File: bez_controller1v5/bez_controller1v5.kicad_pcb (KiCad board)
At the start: 4 copper layers, 130 x 65 mm, 88 parts, among them J1 Conn_01x03_Male, J10 Conn_01x07_Socket, J11 Conn_01x03_Male, J12 Conn_01x03_Male, J13 USB_B_Mini, J14 PPTC041LGBN-RC, J15 Conn_01x03_Male, J16 MOLEX_Conn_Button, J17 MOLEX_Conn_Button, J2 Conn_01x03_Male, J3 Conn_01x03_Male, J4 Screw_Terminal_01x02, J5 Conn_01x03_Male, J6 Conn_01x03_Male, J7 Conn_01x03_Male, J8 JTAG Conn_01x06_Male, J9 Conn_01x09_Socket, U10 USBLC6-4SC6, U11 74LVC2G241, U12 74LVC2G241, U2 74LVC2G241, U3 74LVC2G241, U4 LF50ABV_TO220, U5 LD1117AS33TR_SOT223, U6 INA180A1, U7 STM32F446RETx, U8 74LVC2G241, U9 74LVC2G241, Y1 8MHz

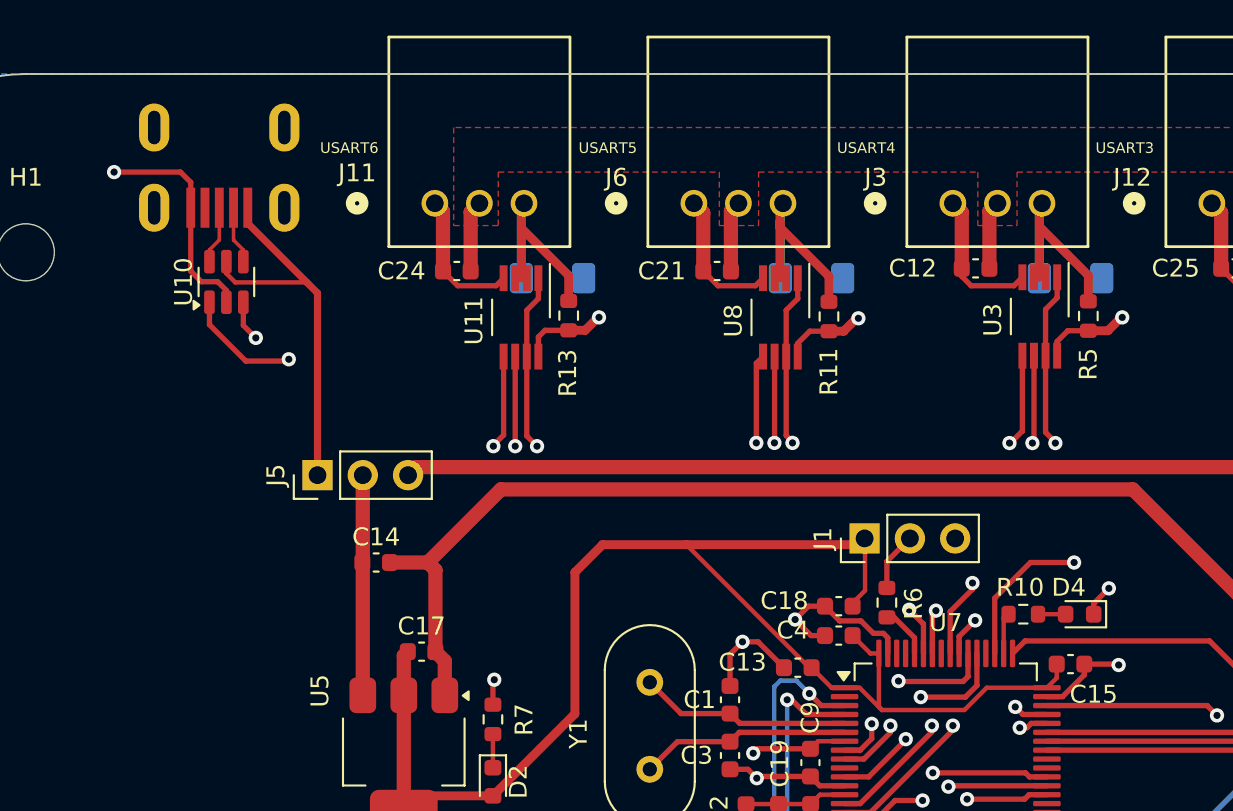
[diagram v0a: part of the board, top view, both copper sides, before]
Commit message: Verified circuit; also added button as per Nam's request
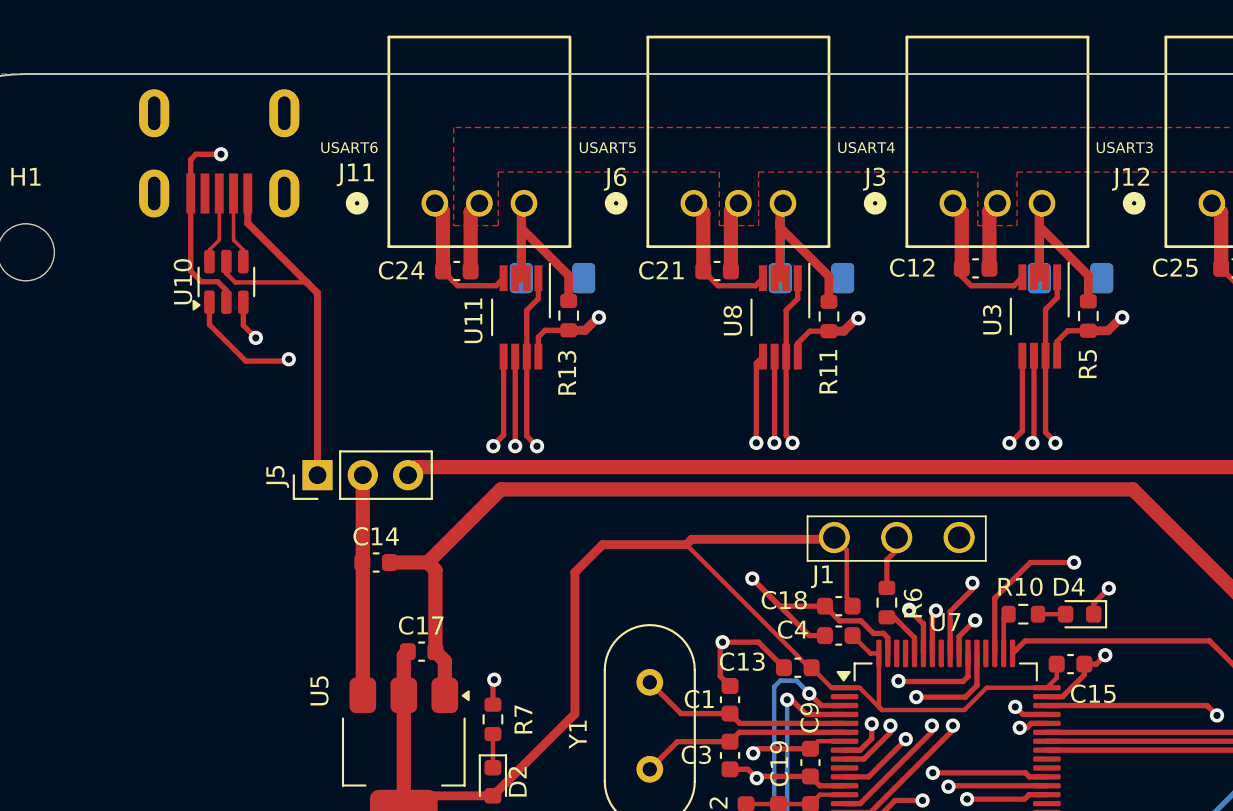
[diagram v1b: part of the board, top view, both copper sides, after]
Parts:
- J1: footprint Connector_PinHeader_2.54mm:PinHeader_1x03_P2.54mm_Vertical -> KiCad:BootloaderButton
- moved J1 3.30 mm to (142.6, 71.8), turned to 0 degrees
- moved J13 0.80 mm to (104.6, 47.1)
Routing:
- net GND: track 125.5 -> 130.7 mm
- net /USART1_DIR: track 64.7 -> 66.0 mm
- net +3.3V: track 299.7 -> 298.6 mm
- net /USART3_RX: track 37.0 -> 36.0 mm

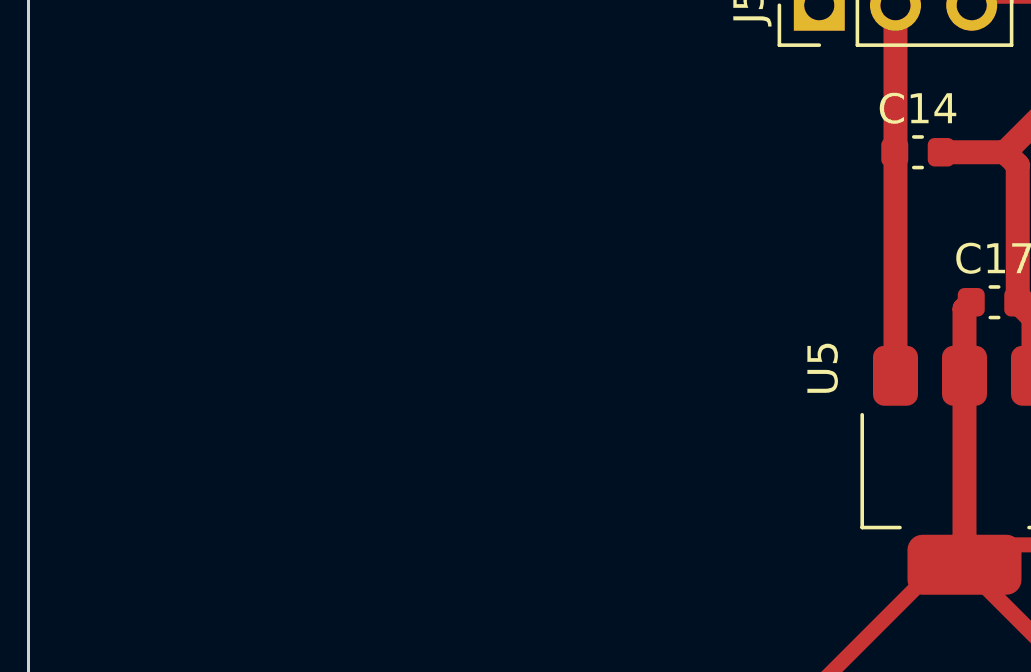
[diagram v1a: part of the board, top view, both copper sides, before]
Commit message: Adding the footprint for the button. Also cleaned up repo (for manufacturing files). Added .gitignore
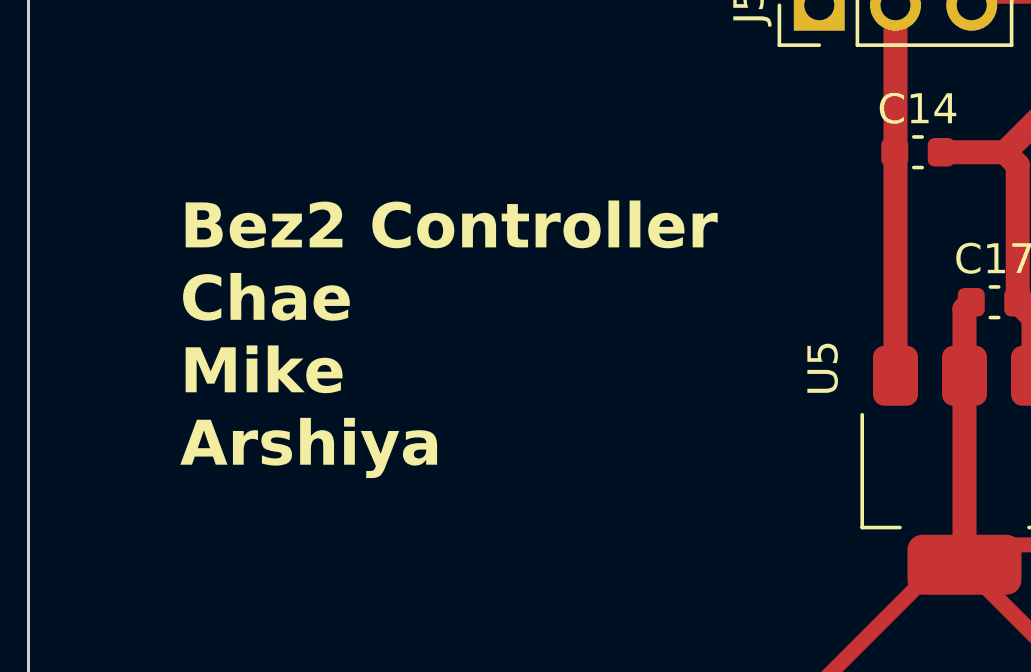
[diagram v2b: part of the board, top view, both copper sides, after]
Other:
- board text added: "Bez2 Controller Chae Mike Arshiya"
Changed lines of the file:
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@@
 		(layer "Edge.Cuts")
+	)
+	(gr_text "Bez2 Controller\nChae\nMike\nArshiya"
+		(at 88.8 81 0)
+		(layer "F.SilkS")
+		(effects
+			(font
+				(size 1.5 1.5)
+				(thickness 0.3)
+				(bold yes)
+			)
+			(justify left bottom)
+		)
 	)
 	(gr_text "U1"

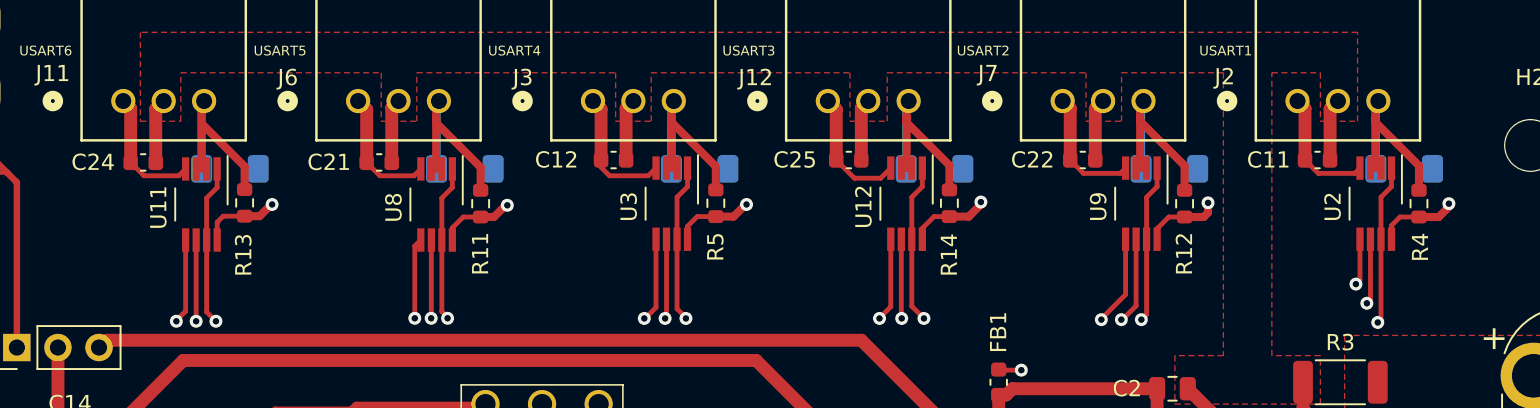
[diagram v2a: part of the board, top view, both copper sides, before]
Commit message: Put zener diodes back on front of the board
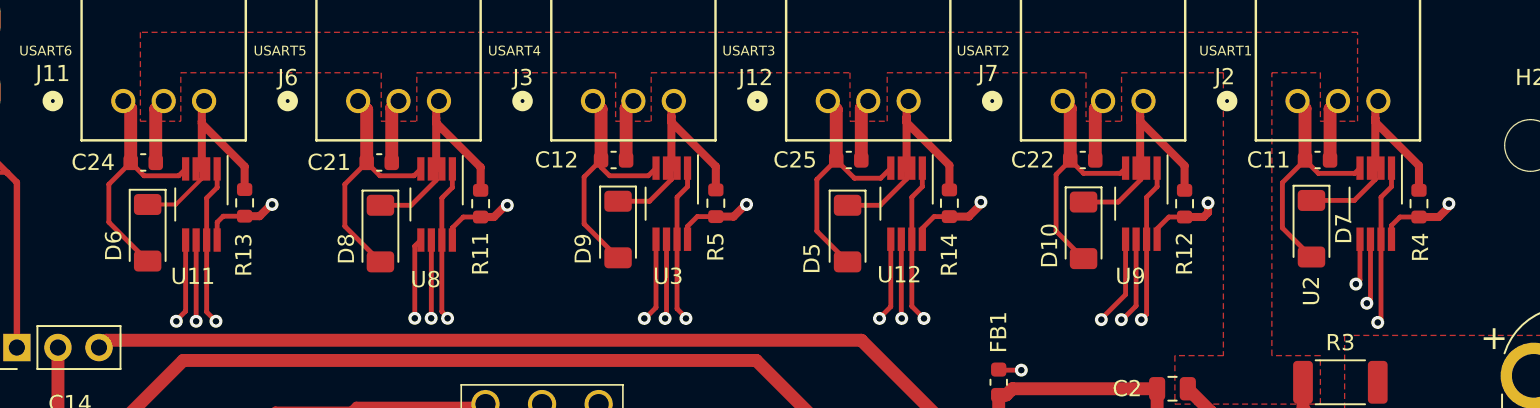
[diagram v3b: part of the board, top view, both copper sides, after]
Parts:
- D10, D5, D6, D7, D8, D9: moved to F.Cu
- moved D7 6.83 mm to (190.2, 58.1), turned to -90 degrees
- moved D5 6.70 mm to (161.5, 58.5), turned to -90 degrees
- moved D8 6.58 mm to (132.6, 58.5), turned to -90 degrees
- moved D10 6.53 mm to (176.1, 58.2), turned to -90 degrees
- moved D6 6.44 mm to (118.2, 58.4), turned to -90 degrees
- moved D9 6.29 mm to (147.3, 58.2), turned to -90 degrees
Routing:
- net GND: track 130.7 -> 175.4 mm
- net /MOTOR_DATA1: track 14.7 -> 15.7 mm
- net /MOTOR_DATA3: track 14.7 -> 15.5 mm
- net /MOTOR_DATA2: track 14.9 -> 15.5 mm
- net /MOTOR_DATA5: track 14.8 -> 15.3 mm

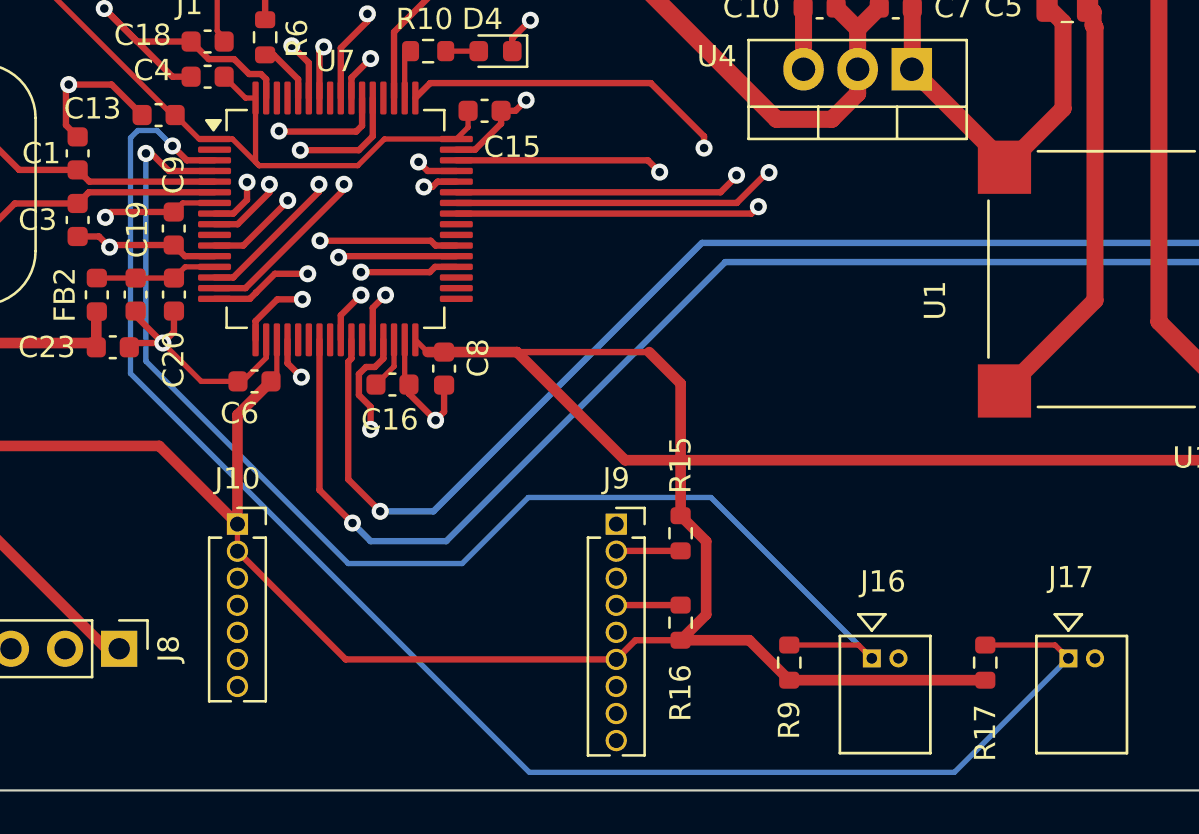
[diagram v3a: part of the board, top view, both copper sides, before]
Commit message: Moved a trace away from edge
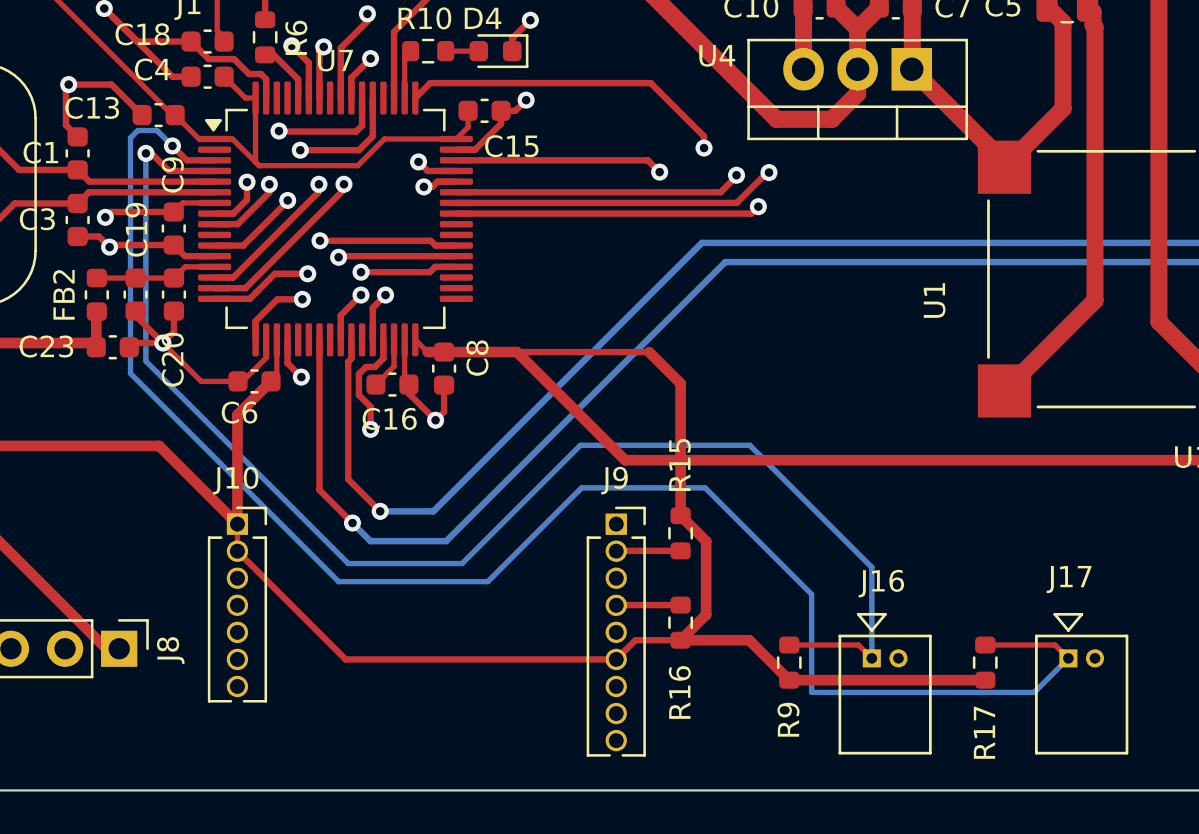
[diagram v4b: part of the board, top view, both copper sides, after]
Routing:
- net /GPIO1: track 60.0 -> 64.5 mm
- net /GPIO2: track 73.9 -> 77.1 mm
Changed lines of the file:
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@@
 			(drillshape 0)
 			(scaleselection 1)
-			(outputdirectory "manufacturing/")
+			(outputdirectory "Manufacturing/")
 		)
 	)
@@
 	)
 	(segment
-		(start 136.455331 87.855331)
-		(end 145.95 97.35)
+		(start 136.455331 78.1)
+		(end 136.455331 87.855331)
 		(width 0.25)
 		(layer "B.Cu")
@@
 	)
 	(segment
-		(start 162.975002 94.25)
-		(end 170.525001 101.799999)
+		(start 156.85 91.8)
+		(end 164.8 91.8)
 		(width 0.25)
 		(layer "B.Cu")
@@
 	)
 	(segment
-		(start 145.95 97.35)
-		(end 151.3 97.35)
+		(start 136.455331 87.855331)
+		(end 145.95 97.35)
 		(width 0.25)
 		(layer "B.Cu")
@@
 	)
 	(segment
-		(start 154.4 94.25)
-		(end 162.975002 94.25)
+		(start 151.3 97.35)
+		(end 156.85 91.8)
 		(width 0.25)
 		(layer "B.Cu")
@@
 	)
 	(segment
-		(start 151.3 97.35)
-		(end 154.4 94.25)
+		(start 164.8 91.8)
+		(end 170.525001 97.525001)
 		(width 0.25)
 		(layer "B.Cu")
@@
 	)
 	(segment
-		(start 136.455331 78.1)
-		(end 136.455331 87.855331)
+		(start 145.95 97.35)
+		(end 151.3 97.35)
+		(width 0.25)
+		(layer "B.Cu")
+		(net 73)
+	)
+	(segment
+		(start 170.525001 97.525001)
+		(end 170.525001 101.799999)
 		(width 0.25)
 		(layer "B.Cu")
@@
 	)
 	(segment
+		(start 156.9 93.8)
+		(end 162.7 93.8)
+		(width 0.25)
+		(layer "B.Cu")
+		(net 74)
+	)
+	(segment
+		(start 135.730331 88.430331)
+		(end 145.5 98.2)
+		(width 0.25)
+		(layer "B.Cu")
+		(net 74)
+	)
+	(segment
+		(start 167.7 103.4)
+		(end 178.15 103.4)
+		(width 0.25)
+		(layer "B.Cu")
+		(net 74)
+	)
+	(segment
+		(start 162.7 93.8)
+		(end 167.7 98.8)
+		(width 0.25)
+		(layer "B.Cu")
+		(net 74)
+	)
+	(segment
 		(start 135.730331 77.369669)
-		(end 136.075 77.025)
+		(end 135.730331 88.430331)
 		(width 0.25)
 		(layer "B.Cu")
@@
 	)
 	(segment
-		(start 174.4 107.15)
-		(end 154.45 107.15)
+		(start 167.7 98.8)
+		(end 167.7 103.4)
 		(width 0.25)
 		(layer "B.Cu")
@@
 	)
 	(segment
-		(start 179.750002 101.799998)
-		(end 174.4 107.15)
+		(start 137.7 77.75)
+		(end 136.975 77.025)
 		(width 0.25)
 		(layer "B.Cu")
@@
 	(segment
 		(start 136.975 77.025)
-		(end 137.7 77.75)
+		(end 136.075 77.025)
 		(width 0.25)
 		(layer "B.Cu")
@@
 	)
 	(segment
-		(start 136.075 77.025)
-		(end 136.975 77.025)
+		(start 152.5 98.2)
+		(end 156.9 93.8)
 		(width 0.25)
 		(layer "B.Cu")
@@
 	)
 	(segment
-		(start 135.730331 88.430331)
+		(start 136.075 77.025)
 		(end 135.730331 77.369669)
 		(width 0.25)
@@
 	)
 	(segment
-		(start 154.45 107.15)
-		(end 135.730331 88.430331)
+		(start 178.15 103.4)
+		(end 179.750002 101.799998)
+		(width 0.25)
+		(layer "B.Cu")
+		(net 74)
+	)
+	(segment
+		(start 145.5 98.2)
+		(end 152.5 98.2)
 		(width 0.25)
 		(layer "B.Cu")
